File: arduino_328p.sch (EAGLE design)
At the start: 15 parts, among them J1 POWER_JACKPTH_LOCK, J2 AVR_SPI_PROG_3X2PTH, J3 6_PIN_SERIAL_CABLEPTH, U1 328P

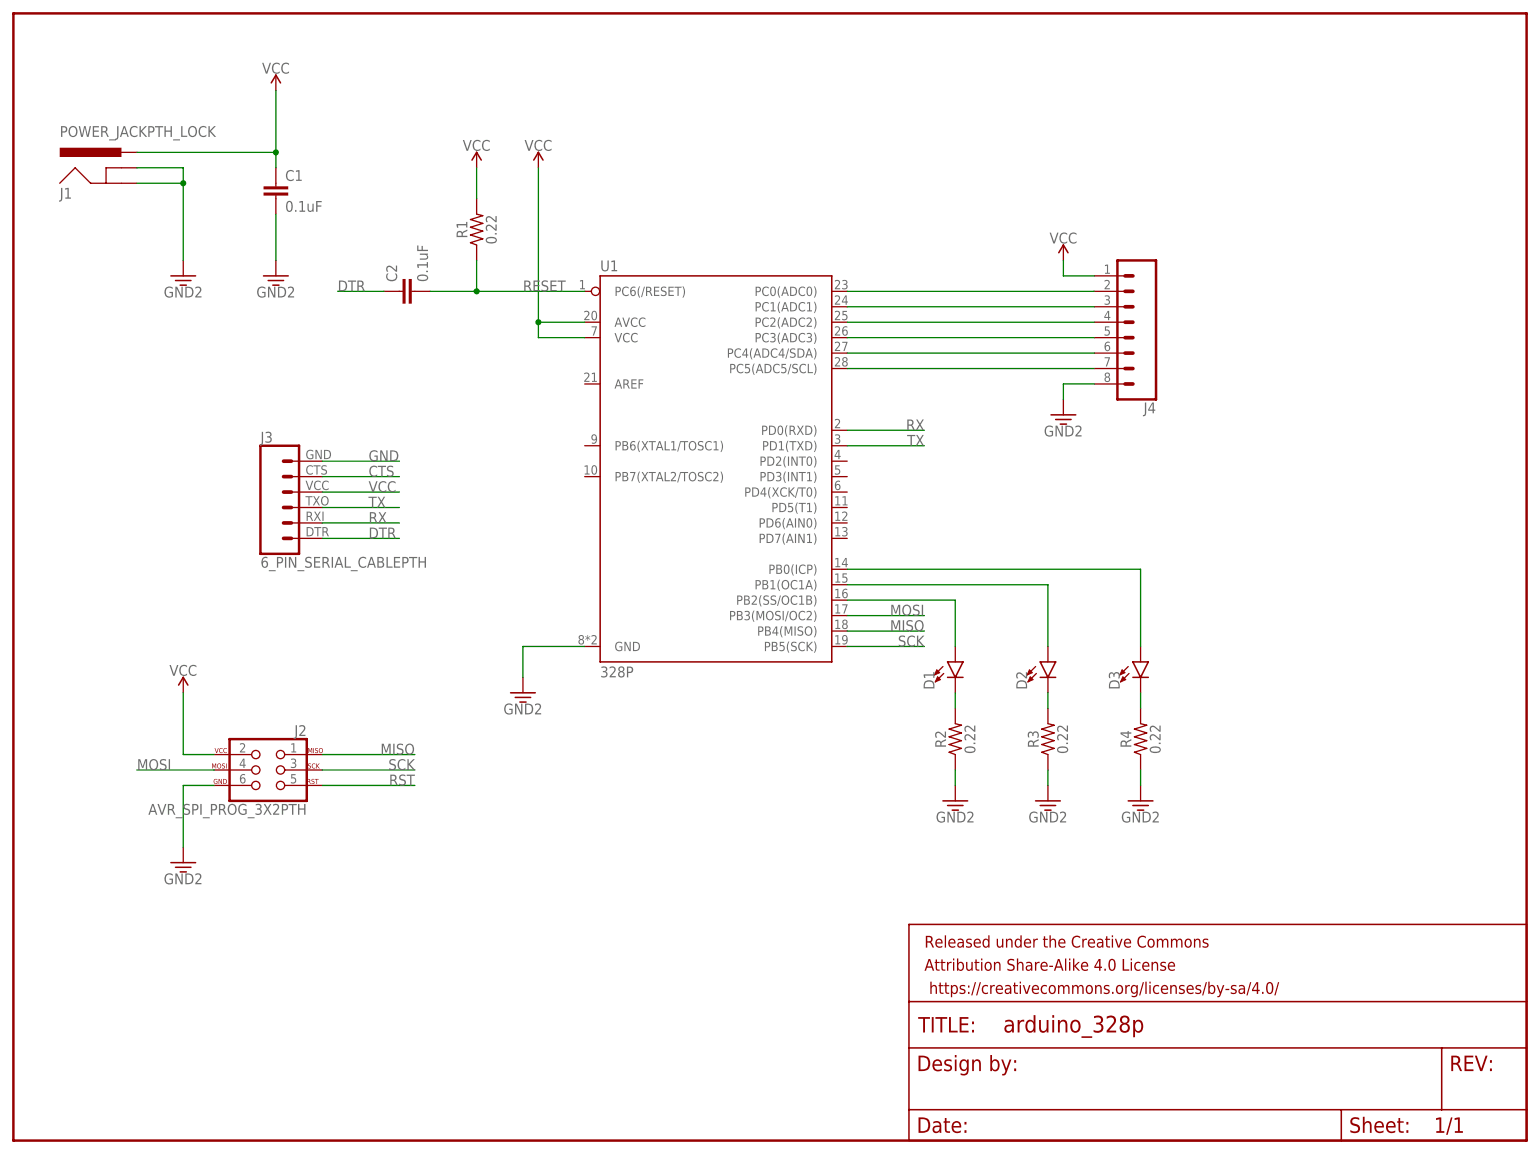
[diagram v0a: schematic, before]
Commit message: replace serial connector
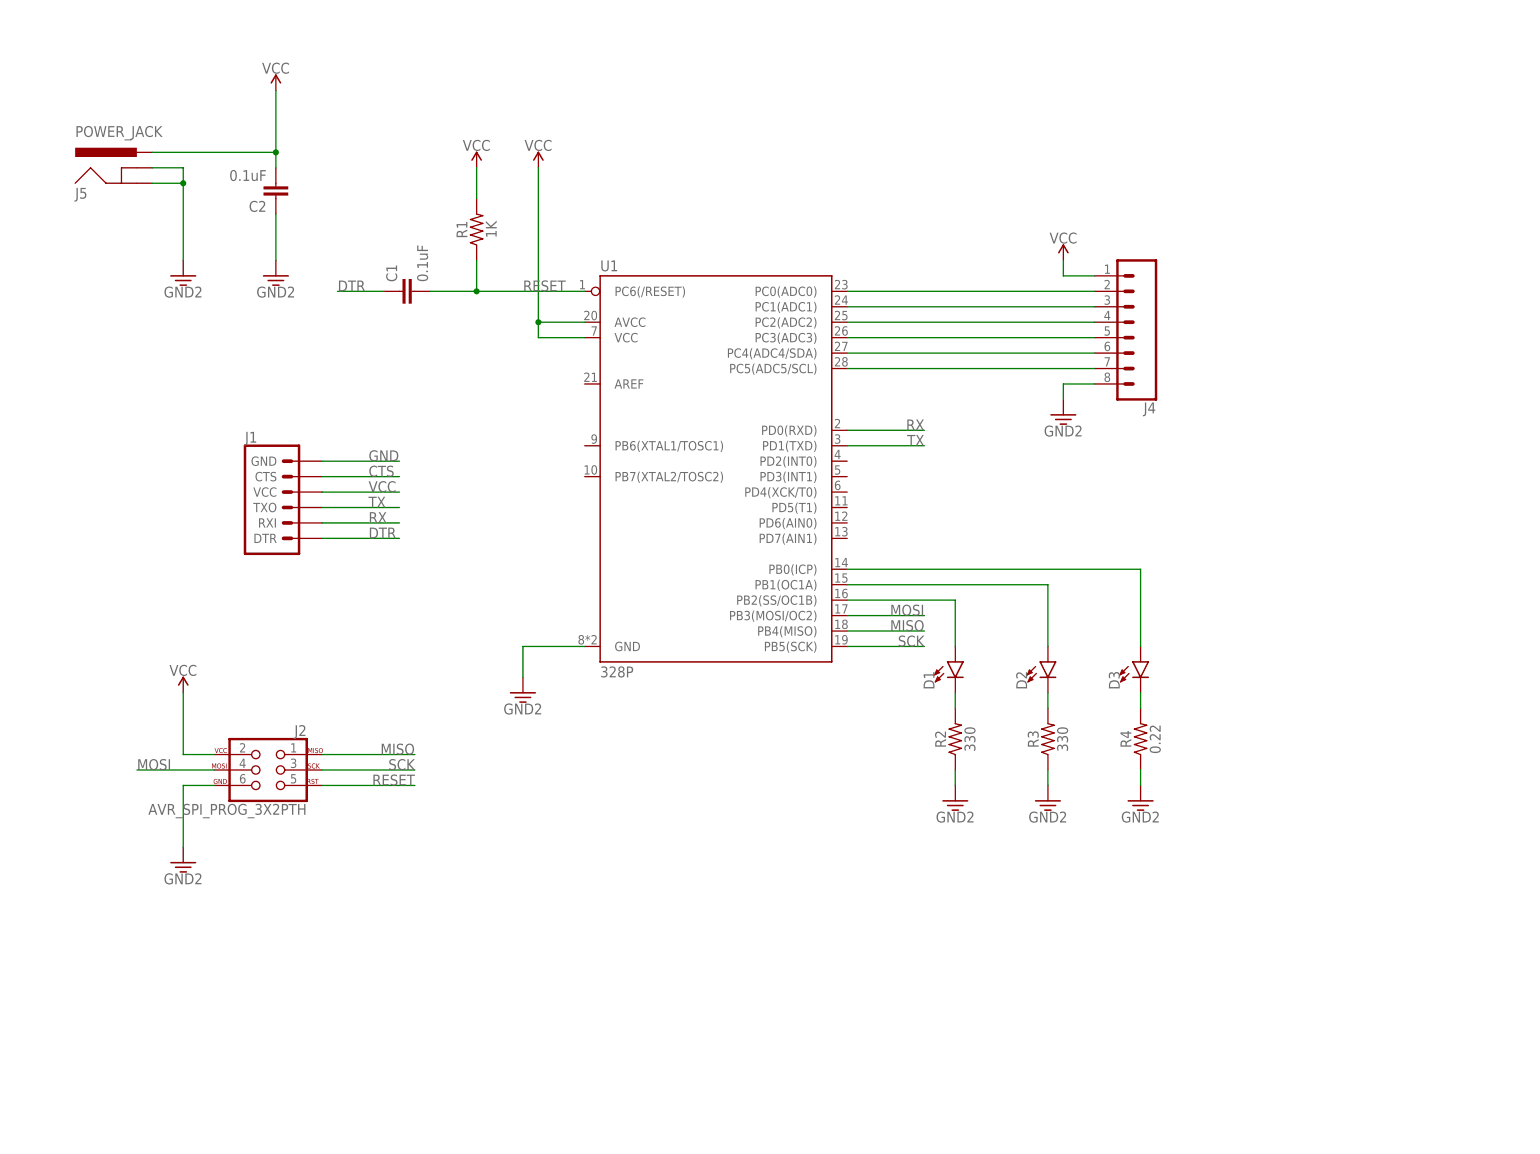
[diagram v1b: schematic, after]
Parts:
- removed FRAME1: FRAME-LETTER, SparkFun-Aesthetics:FRAME-LETTER
- removed J3: 6_PIN_SERIAL_CABLEPTH, SparkFun-Connectors:6_PIN_SERIAL_CABLEPTH
- added J5: POWER_JACK, SparkFun-Connectors:POWER_JACK
- C1, C2: device SparkFun-Capacitors:0.1UF-KIT-EZ-50V-20% -> SparkFun-Capacitors:0.1UF-0402-6.3V-10%-X7R
- D1, D2, D3: device SparkFun-LED:LED5MM -> SparkFun-LED:LED1206
- J1: value POWER_JACKPTH_LOCK -> (none); device SparkFun-Connectors:POWER_JACKPTH_LOCK -> SparkFun-Connectors:6_PIN_SERIAL_TARGETPTH-KIT
- R1: value 0.22 -> 1K
- R2, R3: value 0.22 -> 330
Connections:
- removed net 3.3V: C1.2, J1.GND, J1.GNDBREAK, J2.6, J4.8, R2.1, R3.1, R4.1, U1.GND
- removed net RST: J2.5
- net CTS: now also J1.CTS; no longer J3.5
- net DTR: now also C1.1, J1.DTR; no longer C2.1, J3.1
- net GND: now also C2.1, J1.GND, J2.6, J4.8, J5.GND, J5.GNDBREAK, R2.1, R3.1, R4.1, U1.GND; no longer J3.6
- net RESET: now also C1.2, J2.5; no longer C2.2
- net RX: now also J1.RXI; no longer J3.2
- net TX: now also J1.TXO; no longer J3.3
- net VCC: now also C2.2, J1.VCC, J5.PWR; no longer C1.1, J1.PWR, J3.4
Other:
- moved on the sheet: C1, C2

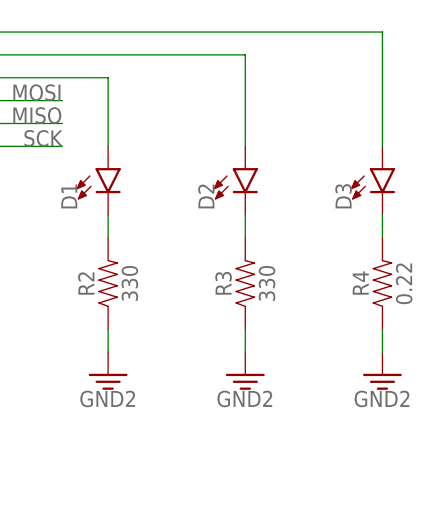
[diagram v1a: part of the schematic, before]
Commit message: change current limit resistor to 330
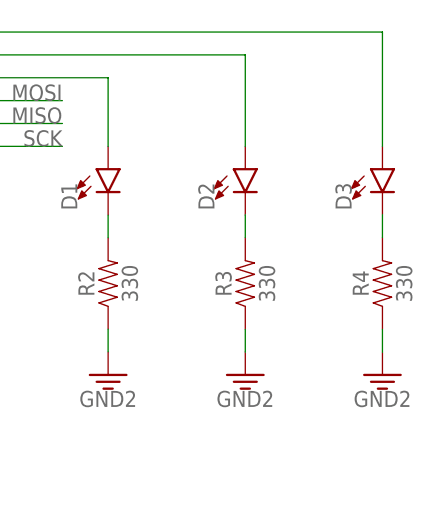
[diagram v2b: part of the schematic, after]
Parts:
- R4: value 0.22 -> 330
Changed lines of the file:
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@@
 <part name="R2" library="SparkFun-Resistors" deviceset="0.22OHM" device="-0805-1/4W-1%" value="330"/>
 <part name="R3" library="SparkFun-Resistors" deviceset="0.22OHM" device="-0805-1/4W-1%" value="330"/>
-<part name="R4" library="SparkFun-Resistors" deviceset="0.22OHM" device="-0805-1/4W-1%" value="0.22"/>
+<part name="R4" library="SparkFun-Resistors" deviceset="0.22OHM" device="-0805-1/4W-1%" value="330"/>
 <part name="J5" library="SparkFun-Connectors" deviceset="POWER_JACK" device=""/>
 <part name="D1" library="SparkFun-LED" deviceset="LED" device="1206"/>
